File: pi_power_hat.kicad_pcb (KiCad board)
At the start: 2 copper layers, 100 x 30 mm, 19 parts, among them J1 GPIO_CONNECTOR, J3 PIR Motion Sensor, J4 DH22T, Q1 DMG1012UW-7

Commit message: Update pi_power_hat.kicad_pcb
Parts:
- added J2: Barrel_Jack, CON-SOCJ-2155:GRAVITECH_CON-SOCJ-2155, F.Cu at (99.6, 113.6)
- added J5: Screw_Terminal_01x02, CONN-TH_P5.00_KF301-5.0-2P:CONN-TH_P5.00_KF301-5.0-2P, F.Cu at (111.0, 117.3)
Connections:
- D1 pad 3: (no net) -> /IN-
- D1 pad 4: (no net) -> /IN+
- J1 pad 10: (no net) -> /GPIO15_RXD0
- J1 pad 11: (no net) -> /GPIO17_GEN0
- J1 pad 12: (no net) -> /GPIO18_GEN1
- J1 pad 13: (no net) -> /GPIO27_GEN2
- J1 pad 15: (no net) -> /GPIO22_GEN3
- J1 pad 16: (no net) -> /GPIO23_GEN4
- J1 pad 18: (no net) -> /GPIO24_GEN5
- J1 pad 19: (no net) -> /GPIO10_SPI_MOSI
- J1 pad 21: (no net) -> /GPIO9_SPI_MISO
- J1 pad 22: (no net) -> /GPIO25_GEN6
- J1 pad 23: (no net) -> /GPIO11_SPI_SCLK
- J1 pad 24: (no net) -> /GPIO8_SPI_CE0_N
- J1 pad 26: (no net) -> /GPIO7_SPI_CE1_N
- J1 pad 27: (no net) -> /ID_SD
- J1 pad 28: (no net) -> /ID_SC
- J1 pad 29: (no net) -> /GPIO5
- J1 pad 3: (no net) -> /GPIO2_SDA1
- J1 pad 31: (no net) -> /GPIO6
- J1 pad 32: (no net) -> /GPIO12
- J1 pad 36: (no net) -> /GPIO16
- J1 pad 38: (no net) -> /GPIO20
- J1 pad 40: (no net) -> /GPIO21
- J1 pad 5: (no net) -> /GPIO3_SCL1
- J1 pad 7: (no net) -> /GPIO4_GPIO_GCLK
- J1 pad 8: (no net) -> /GPIO14_TXD0
- J3 pad 3: (no net) -> Net-(J3-Pad3)
- J4 pad 3: (no net) -> Net-(J4-Pad3)
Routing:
- net /IN-: track 0.00 -> 38.5 mm
- net /IN+: track 0.00 -> 32.0 mm
- net GND: vias 111 -> 191
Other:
- board size 100 x 30 mm -> 92.5 x 30 mm
- board text added: "+"
- board text added: "-"

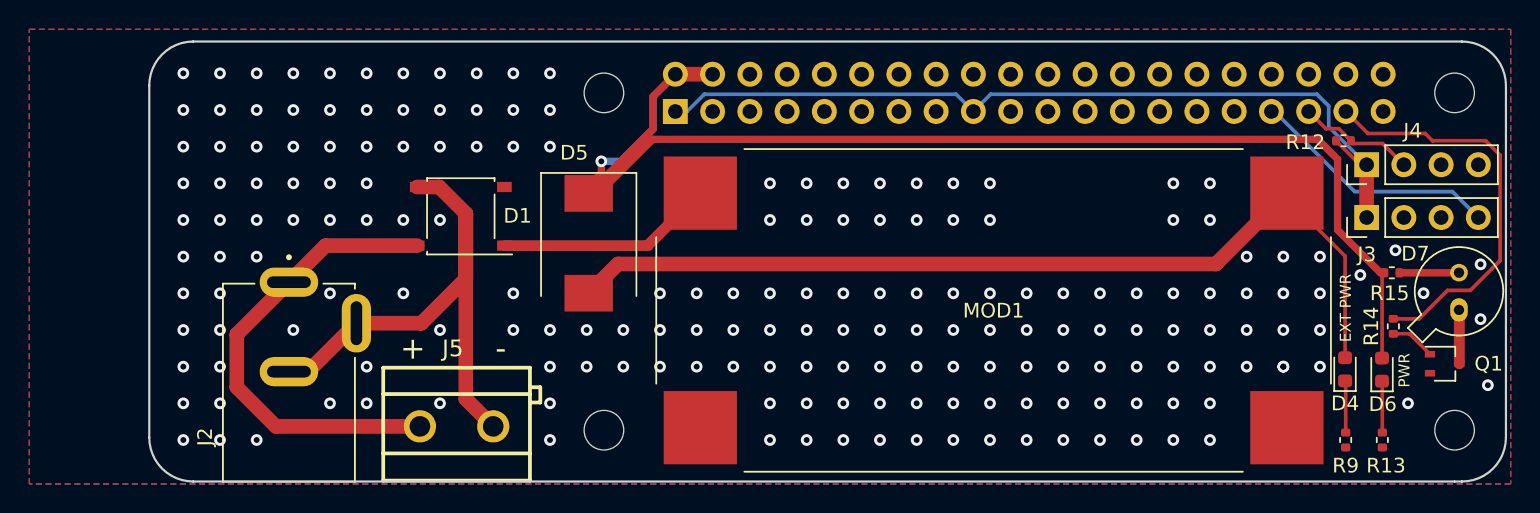
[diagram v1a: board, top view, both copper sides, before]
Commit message: Add fuse
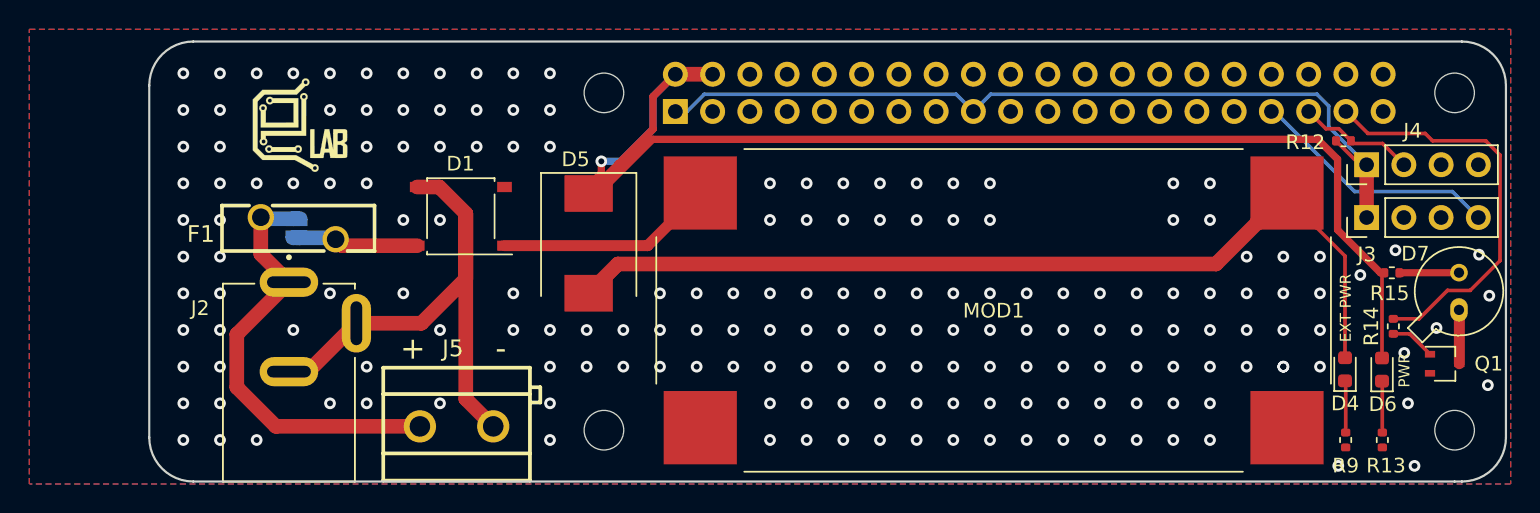
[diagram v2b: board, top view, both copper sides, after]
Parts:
- added F1: Polyfuse, FUSE-TH_L10.4-W3.1-P5.10-D0.8-S1.50:FUSE-TH_L10.4-W3.1-P5.10-D0.8-S1.50, F.Cu at (100.2, 103.8)
- added G***: LOGO, user-footprints:LOGO_eLAB_c=8,1mm, F.Cu at (100.2, 96.8)
- added JP1: Bipass Fuse, Jumper:SolderJumper-2_P1.3mm_Open_RoundedPad1.0x1.5mm, B.Cu at (100.1, 103.8)
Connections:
- D1 pad 4: /IN+ -> Net-(D1-Pad4)
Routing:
- net Net-(D1-Pad4): track 0.00 -> 8.45 mm
- net /IN+: track 32.0 -> 29.9 mm
- net GND: vias 191 -> 184

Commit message: Update pi_power_hat.kicad_pcb
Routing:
- net GND: vias 184 -> 188
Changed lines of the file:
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@@
     (thickness 1.6)
     (drawings 23)
-    (tracks 279)
+    (tracks 283)
     (zones 0)
     (modules 24)
@@
   (via (at 176.3 120) (size 0.8) (drill 0.4) (layers F.Cu B.Cu) (net 2))
   (via (at 181.4 108.4) (size 0.8) (drill 0.4) (layers F.Cu B.Cu) (net 2))
+  (via (at 117.4 103.4) (size 0.8) (drill 0.4) (layers F.Cu B.Cu) (net 2))
+  (via (at 117.4 103.4) (size 0.8) (drill 0.4) (layers F.Cu B.Cu) (net 2))
+  (via (at 124 100) (size 0.8) (drill 0.4) (layers F.Cu B.Cu) (net 2))
+  (via (at 123.4 103.3) (size 0.8) (drill 0.4) (layers F.Cu B.Cu) (net 2))
   (segment (start 166.756 95.838) (end 166.542 95.838) (width 0.25) (layer B.Cu) (net 3))
   (segment (start 172.218 101.3) (end 166.756 95.838) (width 0.25) (layer B.Cu) (net 3))
@@
   (segment (start 173.121 97.337) (end 177.027998 97.337) (width 0.25) (layer F.Cu) (net 5))
   (segment (start 171.622 95.838) (end 173.121 97.337) (width 0.25) (layer F.Cu) (net 5))
-  (segment (start 124.013 104.987) (end 127.6 101.4) (width 0.75) (layer F.Cu) (net 6))
-  (segment (start 114.25 104.987) (end 124.013 104.987) (width 0.75) (layer F.Cu) (net 6))
+  (segment (start 124.013 104.987) (end 127.6 101.4) (width 1) (layer F.Cu) (net 6))
+  (segment (start 114.25 104.987) (end 124.013 104.987) (width 1) (layer F.Cu) (net 6))
   (segment (start 171.605 114.2478) (end 171.5604 114.2032) (width 0.25) (layer F.Cu) (net 7))
   (segment (start 171.605 117.727) (end 171.605 114.2478) (width 0.25) (layer F.Cu) (net 7))
@@
       )
     )
+  )
+  (zone (net 0) (net_name "") (layer F.Cu) (hatch edge 0.508)
+    (connect_pads (clearance 0.508))
+    (min_thickness 0.254)
+    (keepout (tracks allowed) (vias allowed) (copperpour not_allowed))
+    (fill (arc_segments 32) (thermal_gap 0.508) (thermal_bridge_width 0.508))
+    (polygon
+      (pts
+        (xy 130.6 105.4) (xy 124.8 105.4) (xy 130.6 98.4)
+      )
+    )
